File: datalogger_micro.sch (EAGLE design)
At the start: 46 parts, among them IC1 DS3231/SO, IC3 LD117AS33TR, M0 PAT, M1 PAT, Q4 IRLML5203

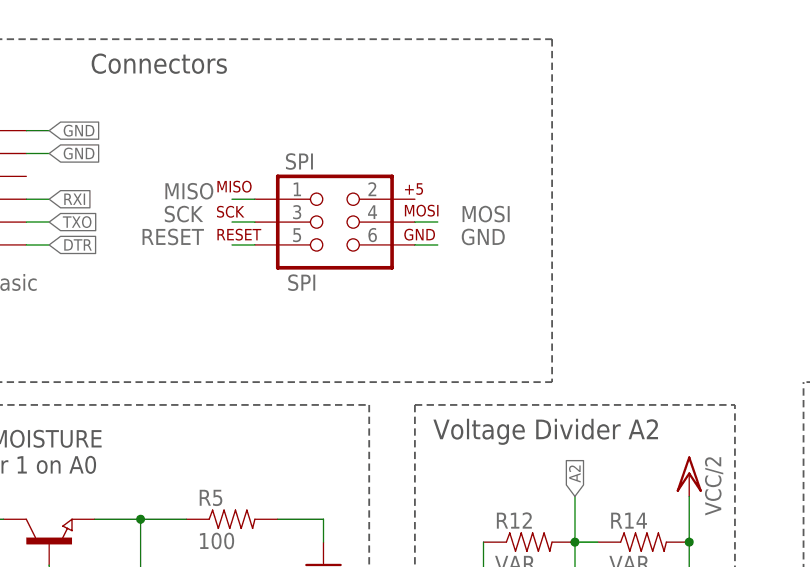
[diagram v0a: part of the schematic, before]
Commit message: pre 0.95
Board finalized. Will be printed after last quality check.
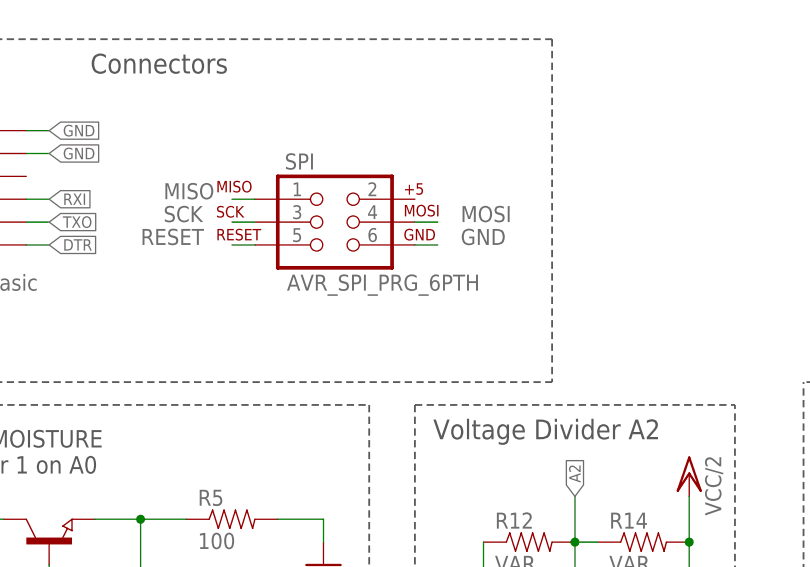
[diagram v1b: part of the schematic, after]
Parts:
- SPI: value SPI -> AVR_SPI_PRG_6PTH; device SparkFun-Connectors:AVR_SPI_PRG_62X3_LOCK -> SparkFun-Connectors:AVR_SPI_PRG_6PTH
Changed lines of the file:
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@@
 <?xml version="1.0" encoding="utf-8"?>
 <!DOCTYPE eagle SYSTEM "eagle.dtd">
-<eagle version="7.2.0">
+<eagle version="7.3.0">
 <drawing>
 <settings>
@@
 <part name="C3" library="SparkFun" deviceset="CAP" device="1206" value="10uF"/>
 <part name="POWER" library="SparkFun" deviceset="M02" device="PTH"/>
-<part name="SPI" library="SparkFun-Connectors" deviceset="AVR_SPI_PRG_6" device="2X3_LOCK" value="SPI"/>
+<part name="SPI" library="SparkFun-Connectors" deviceset="AVR_SPI_PRG_6" device="PTH"/>
 </parts>
 <sheets>
@@
 </segment>
 <segment>
-<pinref part="SPI" gate="G$1" pin="6"/>
 <wire x1="78.74" y1="101.6" x2="76.2" y2="101.6" width="0.1524" layer="91"/>
 <label x="81.28" y="101.6" size="1.778" layer="95"/>
+<pinref part="SPI" gate="G$1" pin="6"/>
 </segment>
 </net>
@@
 </segment>
 <segment>
-<pinref part="SPI" gate="G$1" pin="5"/>
 <wire x1="55.88" y1="101.6" x2="58.42" y2="101.6" width="0.1524" layer="91"/>
 <label x="45.72" y="101.6" size="1.778" layer="95"/>
+<pinref part="SPI" gate="G$1" pin="5"/>
 </segment>
 </net>
@@
 </segment>
 <segment>
-<pinref part="SPI" gate="G$1" pin="1"/>
 <wire x1="58.42" y1="106.68" x2="55.88" y2="106.68" width="0.1524" layer="91"/>
 <label x="48.26" y="106.68" size="1.778" layer="95"/>
+<pinref part="SPI" gate="G$1" pin="1"/>
 </segment>
 </net>

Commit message: bug fix
A0 had no connection to sensor
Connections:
- removed net PC0: Q2.E, R5.1
- net A0: now also Q2.E, R5.1
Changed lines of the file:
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@@
 <label x="45.72" y="60.96" size="1.27" layer="95" rot="R270" xref="yes"/>
+</segment>
+<segment>
+<pinref part="Q2" gate="G$1" pin="E"/>
+<wire x1="50.8" y1="71.12" x2="45.72" y2="71.12" width="0.1524" layer="91"/>
+<wire x1="45.72" y1="71.12" x2="40.64" y2="71.12" width="0.1524" layer="91"/>
+<wire x1="45.72" y1="71.12" x2="45.72" y2="60.96" width="0.1524" layer="91"/>
+<junction x="45.72" y="71.12"/>
+<pinref part="R5" gate="G$1" pin="1"/>
 </segment>
 </net>
@@
 </segment>
 </net>
-<net name="PC0" class="0">
-<segment>
-<pinref part="Q2" gate="G$1" pin="E"/>
-<wire x1="50.8" y1="71.12" x2="45.72" y2="71.12" width="0.1524" layer="91"/>
-<wire x1="45.72" y1="71.12" x2="40.64" y2="71.12" width="0.1524" layer="91"/>
-<wire x1="45.72" y1="71.12" x2="45.72" y2="60.96" width="0.1524" layer="91"/>
-<junction x="45.72" y="71.12"/>
-<pinref part="R5" gate="G$1" pin="1"/>
-</segment>
-</net>

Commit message: VERSION 0.95
finalized Version 0.95, to be printed
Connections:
- net D10 renamed FLASH_CE
- net D3 renamed INT1
- net D7 renamed RTC_VCC
- net D8 renamed RTC_INT
- removed net A0: ATMEGA328P.PC0(ADC0), Q2.E, R5.1
- removed net A1: ATMEGA328P.PC1(ADC1), Q3.E, R10.1
- removed net A2: ATMEGA328P.PC2(ADC2), R12.2, R14.1, VD2.2
- removed net A3: ATMEGA328P.PC3(ADC3), R13.2, R15.1, VD3.2
- removed net D2: ATMEGA328P.PD2(INT0), IC1./RST
- removed net D4: ATMEGA328P.PD4(XCK/T0), R6.1
- removed net D5: ATMEGA328P.PD5(T1), Q4.G, R8.1
- removed net D6: ATMEGA328P.PD6(AIN0)
- removed net D9: ATMEGA328P.PB1(OC1A)
- new net INT0: ATMEGA328P.PD2(INT0)
- new net LED1: ATMEGA328P.PD5(T1), R6.1
- new net RTC_RST: ATMEGA328P.PC1(ADC1), IC1./RST
- new net SOIL1: ATMEGA328P.ADC7, Q2.E, R5.1
- new net SOIL2: ATMEGA328P.PC2(ADC2), Q3.E, R10.1
- new net VCC/ST_ON: ATMEGA328P.PB1(OC1A), Q4.G, R8.1
- new net VDIV1: ATMEGA328P.PC0(ADC0), R13.2, R15.1, VD3.2
- new net VDIV2: ATMEGA328P.PC3(ADC3), R12.2, R14.1, VD2.2
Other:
- moved on the sheet: R12, R13, R14, R15, VD2, VD3

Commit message: VERSION 0.95 final
final printed Version 0.95 to be published
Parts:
- removed C9: 0.1uF, SparkFun:CAP0603-CAP
- removed Q4: IRLML5203, transistor-power:IRLML5203
- removed U$5: DRUCKTASTER-1PIN, Edu Logger Basic Components:DRUCKTASTER-1PIN
- removed VD3: PAT, SparkFun:M02PTH
- added C2: 0.1uF, SparkFun:CAP0603-CAP
- added Q1: (no value), semicon-smd-ipc:NPN-TRANSISTOR_SOT23
- added U$3: SST25VF032B, SST25:SST25VF032B
- added VD1: PAT, SparkFun:M02PTH
- C3: value 10uF -> 0.1uF; device SparkFun:CAP1206 -> SparkFun:CAP0603-CAP
- C7: value 0.1uF -> 10uF; device SparkFun:CAP0603-CAP -> SparkFun:CAP1206
- Q2: value (none) -> IRLML5203; device semicon-smd-ipc:NPN-TRANSISTOR_SOT23 -> transistor-power:IRLML5203
- R10: value 100 -> 10k
- R11: value 470 -> 100K
- R12: value VAR -> 100k
- R13, R17: value VAR -> 100
- R16: value VAR -> 470
- R18: value 10k -> 470
- R5, R9: value 100 -> VAR
- R6: value 470 -> VAR
- R7: value 100K -> 100
- R8: value 100k -> VAR
- U$2: value SST25VF032B -> DRUCKTASTER-1PIN; device SST25:SST25VF032B -> Edu Logger Basic Components:DRUCKTASTER-1PIN
- renumbered C8 to C5, D3 to D1, IC3 to IC2, M0 to M2, U$4 to U$100
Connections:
- net A5: now also R2.1; no longer R3.1
- net A6: now also R8.2, R9.2; no longer R16.2, R17.2
- net DTR: now also C2.2; no longer C4.2
- net FLASH_CE: now also R11.2, U$3.CE#; no longer R7.2, U$2.CE#
- net GND: now also C3.1, C4.1, C7.2, Q2.D, R12.2, R15.1, R17.2, R6.1, R7.2, R9.1, U$2.2, U$3.VSS; no longer C3.2, C7.1, C9.1, Q4.D, R10.2, R12.1, R13.1, R17.1, R5.2, R8.2, U$2.VSS, U$5.2
- net GNDA: now also U$2.1; no longer U$5.1
- net LED1: now also R16.1; no longer R6.1
- net MISO: now also U$3.SO; no longer U$2.SO
- net MOSI: now also U$3.SI; no longer U$2.SI
- net N$1: now also Q2.S; no longer Q4.S
- net N$4: now also R18.1; no longer R11.1
- net N$5: now also Q1.B; no longer Q3.B
- net N$6: now also Q3.B; no longer Q2.B
- net N$7: now also R16.2; no longer R6.2
- net N$8: now also R4.2; no longer R9.2
- net N$9: now also R13.2; no longer R4.2
- net RESET: now also C2.1, R3.1; no longer C4.1, R2.1
- net RTC_INT: now also R10.1; no longer R18.1
- net SCK: now also U$3.SCK; no longer U$2.SCK
- net SOIL1: now also Q3.E, R17.1; no longer Q2.E, R5.1
- net SOIL2: now also Q1.E, R7.1; no longer Q3.E, R10.1
- net VBAT: now also C4.2, R10.2, R5.2, R8.1, VD1.1; no longer C7.2, R15.2, R16.1, R18.2, VD3.1
- net VCC-ST: now also C3.2, C7.1, Q1.C, R11.1, R13.1, R18.2, U$3.HOLD#, U$3.VDD, U$3.WP#; no longer C3.1, C9.2, Q2.C, R11.2, R7.1, R9.1, U$2.HOLD#, U$2.VDD, U$2.WP#
- net VCC/ST_ON: now also Q2.G, R12.1; no longer Q4.G, R8.1
- net VDIV1: now also R14.1, R15.2, VD2.2; no longer R13.2, R15.1, VD3.2
- net VDIV2: now also R5.1, R6.2, VD1.2; no longer R12.2, R14.1, VD2.2
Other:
- moved on the sheet: C1, C3, C4, C7, Q3, R10, R11, R12, R13, R14, R15, R16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
